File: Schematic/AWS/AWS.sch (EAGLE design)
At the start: 21 parts, among them J1 WeatherShield, J2 Fan, J3 Valve, J4 FlowMeter, Q1 IRLZ44Z, U1 SN754410_NE_16, X1 16 MHz

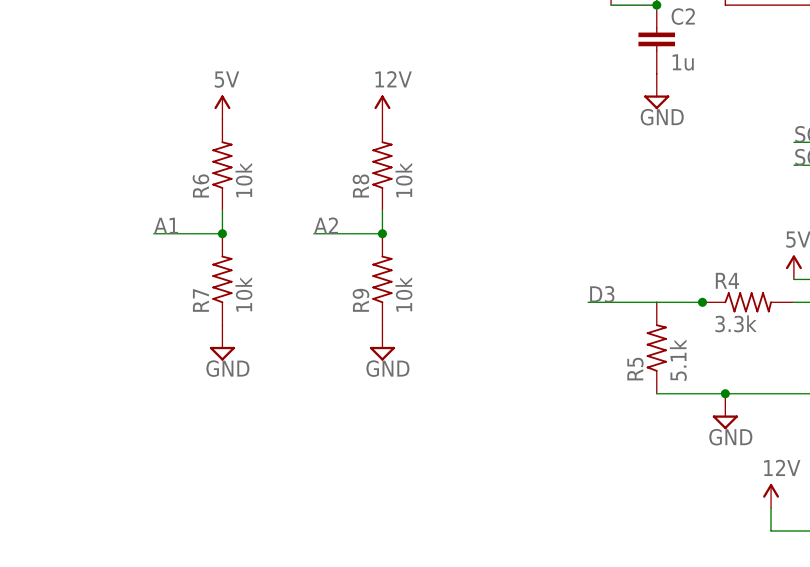
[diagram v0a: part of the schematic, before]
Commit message: Updated Resistor value
And remove .s#* files
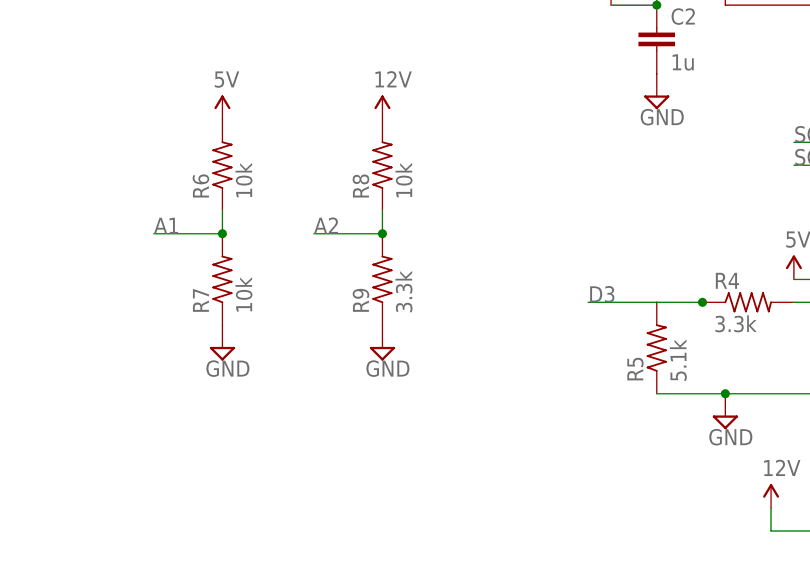
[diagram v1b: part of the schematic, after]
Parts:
- R9: value 10k -> 3.3k
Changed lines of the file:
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@@
 <part name="SUPPLY15" library="SparkFun" deviceset="VCC" device="" value="5V"/>
 <part name="R8" library="rcl" deviceset="R-US_" device="0204/2V" value="10k"/>
-<part name="R9" library="rcl" deviceset="R-US_" device="0204/2V" value="10k"/>
+<part name="R9" library="rcl" deviceset="R-US_" device="0204/2V" value="3.3k"/>
 <part name="SUPPLY16" library="supply2" deviceset="GND" device=""/>
 <part name="SUPPLY17" library="SparkFun" deviceset="VCC" device="" value="12V"/>

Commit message: Fan Working
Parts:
- removed Q1: IRLZ44Z, transistor-power:IRLZ44Z
- removed R3: 330, rcl:R-US_0204/2V
- R7: value 10k -> 2.2k
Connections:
- removed net N$4: J2.3, Q1.D
- removed net N$5: C1.2, U1.GND_1, U1.GND_4
- removed net N$8: Q1.G, R3.2
- new net FAN: J2.2, U1.3Y
- net A0: now also U1.3A; no longer R3.1
- net A1: now also U1.3; no longer R6.1, R7.2
- net A6: now also R6.1, R7.2
- net GND: now also C1.2, J2.3, U1.GND_1, U1.GND_4; no longer Q1.S
- net VCC: no longer J2.1
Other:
- moved on the sheet: C1
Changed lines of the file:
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@@
 <part name="SUPPLY9" library="SparkFun" deviceset="VCC" device="" value="5V"/>
 <part name="SUPPLY10" library="supply2" deviceset="GND" device=""/>
-<part name="Q1" library="transistor-power" deviceset="IRLZ44Z" device=""/>
 <part name="J2" library="con-amp" deviceset="215876-6" device="" value="Fan"/>
-<part name="SUPPLY11" library="SparkFun" deviceset="VCC" device="" value="12V"/>
-<part name="SUPPLY12" library="supply2" deviceset="GND" device=""/>
-<part name="R3" library="rcl" deviceset="R-US_" device="0204/2V" value="330"/>
 <part name="R4" library="rcl" deviceset="R-US_" device="0204/2V" value="3.3k"/>
 <part name="R5" library="rcl" deviceset="R-US_" device="0204/2V" value="5.1k"/>
 <part name="R6" library="rcl" deviceset="R-US_" device="0204/2V" value="10k"/>
-<part name="R7" library="rcl" deviceset="R-US_" device="0204/2V" value="10k"/>
+<part name="R7" library="rcl" deviceset="R-US_" device="0204/2V" value="2.2k"/>
 <part name="SUPPLY13" library="supply2" deviceset="GND" device=""/>
 <part name="SUPPLY15" library="SparkFun" deviceset="VCC" device="" value="5V"/>
@@
 <part name="SUPPLY16" library="supply2" deviceset="GND" device=""/>
 <part name="SUPPLY17" library="SparkFun" deviceset="VCC" device="" value="12V"/>
+<part name="SUPPLY11" library="supply2" deviceset="GND" device=""/>
 </parts>
 <sheets>
@@
 </instance>
 <instance part="U1" gate="A" x="220.98" y="134.62"/>
-<instance part="SUPPLY2" gate="1" x="243.84" y="147.32"/>
+<instance part="SUPPLY2" gate="1" x="248.92" y="147.32"/>
 <instance part="SUPPLY1" gate="GND" x="185.42" y="129.54"/>
-<instance part="SUPPLY3" gate="GND" x="243.84" y="129.54"/>
+<instance part="SUPPLY3" gate="GND" x="248.92" y="132.08"/>
 <instance part="SUPPLY7" gate="1" x="198.12" y="119.38"/>
-<instance part="C1" gate="G$1" x="243.84" y="139.7"/>
+<instance part="C1" gate="G$1" x="248.92" y="139.7"/>
 <instance part="C2" gate="G$1" x="203.2" y="116.84"/>
 <instance part="SUPPLY8" gate="GND" x="203.2" y="109.22"/>
@@
 <instance part="SUPPLY9" gate="1" x="218.44" y="88.9"/>
 <instance part="SUPPLY10" gate="GND" x="210.82" y="73.66"/>
-<instance part="Q1" gate="G$1" x="208.28" y="50.8"/>
 <instance part="J2" gate="G$1" x="228.6" y="55.88"/>
-<instance part="SUPPLY11" gate="1" x="215.9" y="63.5"/>
-<instance part="SUPPLY12" gate="GND" x="210.82" y="43.18"/>
-<instance part="R3" gate="G$1" x="198.12" y="48.26"/>
 <instance part="R4" gate="G$1" x="213.36" y="86.36"/>
 <instance part="R5" gate="G$1" x="203.2" y="81.28" rot="R90"/>
@@
 <instance part="SUPPLY16" gate="GND" x="172.72" y="81.28"/>
 <instance part="SUPPLY17" gate="1" x="172.72" y="106.68"/>
+<instance part="SUPPLY11" gate="GND" x="218.44" y="50.8"/>
 </instances>
 <busses>
@@
 </segment>
 <segment>
-<pinref part="Q1" gate="G$1" pin="S"/>
-<pinref part="SUPPLY12" gate="GND" pin="GND"/>
-</segment>
-<segment>
 <pinref part="R5" gate="G$1" pin="1"/>
 <pinref part="SUPPLY10" gate="GND" pin="GND"/>
@@
 <pinref part="R9" gate="G$1" pin="1"/>
 <pinref part="SUPPLY16" gate="GND" pin="GND"/>
+</segment>
+<segment>
+<pinref part="U1" gate="A" pin="GND_4"/>
+<pinref part="U1" gate="A" pin="GND_1"/>
+<wire x1="238.76" y1="132.08" x2="238.76" y2="134.62" width="0.1524" layer="91"/>
+<wire x1="238.76" y1="134.62" x2="248.92" y2="134.62" width="0.1524" layer="91"/>
+<pinref part="C1" gate="G$1" pin="2"/>
+<junction x="248.92" y="134.62"/>
+<pinref part="SUPPLY3" gate="GND" pin="GND"/>
+</segment>
+<segment>
+<pinref part="J2" gate="G$1" pin="3"/>
+<pinref part="SUPPLY11" gate="GND" pin="GND"/>
+<wire x1="226.06" y1="55.88" x2="218.44" y2="55.88" width="0.1524" layer="91"/>
+<wire x1="218.44" y1="55.88" x2="218.44" y2="53.34" width="0.1524" layer="91"/>
 </segment>
 </net>
@@
 <segment>
 <pinref part="U1" gate="A" pin="VCC1"/>
-<wire x1="238.76" y1="142.24" x2="243.84" y2="142.24" width="0.1524" layer="91"/>
+<wire x1="238.76" y1="142.24" x2="248.92" y2="142.24" width="0.1524" layer="91"/>
 <pinref part="SUPPLY2" gate="1" pin="VCC"/>
-<wire x1="243.84" y1="142.24" x2="243.84" y2="147.32" width="0.1524" layer="91"/>
+<wire x1="248.92" y1="142.24" x2="248.92" y2="147.32" width="0.1524" layer="91"/>
 <pinref part="C1" gate="G$1" pin="1"/>
-<junction x="243.84" y="142.24"/>
+<junction x="248.92" y="142.24"/>
 </segment>
 <segment>
@@
 </segment>
 <segment>
-<pinref part="J2" gate="G$1" pin="1"/>
-<pinref part="SUPPLY11" gate="1" pin="VCC"/>
-<wire x1="226.06" y1="60.96" x2="215.9" y2="60.96" width="0.1524" layer="91"/>
-<wire x1="215.9" y1="60.96" x2="215.9" y2="63.5" width="0.1524" layer="91"/>
-</segment>
-<segment>
 <pinref part="R8" gate="G$1" pin="2"/>
 <pinref part="SUPPLY17" gate="1" pin="VCC"/>
@@
 <pinref part="ATMEGA328" gate="G$1" pin="ADC6"/>
 </segment>
+<segment>
+<pinref part="R6" gate="G$1" pin="1"/>
+<pinref part="R7" gate="G$1" pin="2"/>
+<wire x1="154.94" y1="96.52" x2="154.94" y2="93.98" width="0.1524" layer="91"/>
+<wire x1="154.94" y1="93.98" x2="147.32" y2="93.98" width="0.1524" layer="91"/>
+<junction x="154.94" y="93.98"/>
+<label x="147.32" y="93.98" size="1.778" layer="95"/>
+</segment>
 </net>
 <net name="A4_SDA" class="0">
@@
 </segment>
 <segment>
-<pinref part="R6" gate="G$1" pin="1"/>
-<pinref part="R7" gate="G$1" pin="2"/>
-<wire x1="154.94" y1="96.52" x2="154.94" y2="93.98" width="0.1524" layer="91"/>
-<wire x1="154.94" y1="93.98" x2="147.32" y2="93.98" width="0.1524" layer="91"/>
-<junction x="154.94" y="93.98"/>
-<label x="147.32" y="93.98" size="1.778" layer="95"/>
+<pinref part="U1" gate="A" pin="3"/>
+<wire x1="238.76" y1="124.46" x2="243.84" y2="124.46" width="0.1524" layer="91"/>
+<label x="241.3" y="124.46" size="1.778" layer="95"/>
 </segment>
 </net>
@@
 </segment>
 <segment>
-<pinref part="R3" gate="G$1" pin="1"/>
-<wire x1="193.04" y1="48.26" x2="185.42" y2="48.26" width="0.1524" layer="91"/>
-<label x="185.42" y="48.26" size="1.778" layer="95"/>
+<pinref part="U1" gate="A" pin="3A"/>
+<wire x1="238.76" y1="127" x2="243.84" y2="127" width="0.1524" layer="91"/>
+<label x="241.3" y="127" size="1.778" layer="95"/>
 </segment>
 </net>
@@
 </segment>
 </net>
-<net name="N$5" class="0">
-<segment>
-<pinref part="U1" gate="A" pin="GND_4"/>
-<pinref part="U1" gate="A" pin="GND_1"/>
-<wire x1="238.76" y1="132.08" x2="238.76" y2="134.62" width="0.1524" layer="91"/>
-<wire x1="238.76" y1="134.62" x2="243.84" y2="134.62" width="0.1524" layer="91"/>
-<wire x1="243.84" y1="134.62" x2="243.84" y2="132.08" width="0.1524" layer="91"/>
-<pinref part="C1" gate="G$1" pin="2"/>
-<junction x="243.84" y="134.62"/>
-</segment>
-</net>
 <net name="SOL+" class="0">
 <segment>
@@
 </segment>
 </net>
-<net name="N$4" class="0">
-<segment>
-<pinref part="Q1" gate="G$1" pin="D"/>
-<pinref part="J2" gate="G$1" pin="3"/>
-<wire x1="210.82" y1="55.88" x2="226.06" y2="55.88" width="0.1524" layer="91"/>
-</segment>
-</net>
-<net name="N$8" class="0">
-<segment>
-<pinref part="Q1" gate="G$1" pin="G"/>
-<pinref part="R3" gate="G$1" pin="2"/>
-<wire x1="205.74" y1="48.26" x2="203.2" y2="48.26" width="0.1524" layer="91"/>
-</segment>
-</net>
+<net name="FAN" class="0">
+<segment>
+<pinref part="U1" gate="A" pin="3Y"/>
+<wire x1="238.76" y1="129.54" x2="243.84" y2="129.54" width="0.1524" layer="91"/>
+<label x="241.3" y="129.54" size="1.778" layer="95"/>
+</segment>
+<segment>
+<pinref part="J2" gate="G$1" pin="2"/>
+<wire x1="226.06" y1="58.42" x2="218.44" y2="58.42" width="0.1524" layer="91"/>
+<label x="218.44" y="58.42" size="1.778" layer="95"/>
+</segment>
+</net>

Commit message: All Basic Functions Working!
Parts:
- added R3: 10k, rcl:R-US_0204/2V
- R4: value 3.3k -> 10k
- R5: value 5.1k -> 3.3k
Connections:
- net D3: now also R3.1
- net VCC: now also R3.2
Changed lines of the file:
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@@
 <part name="J3" library="con-amp" deviceset="215876-6" device="" value="Valve"/>
 <part name="J4" library="con-amp" deviceset="215876-6" device="" value="FlowMeter"/>
-<part name="SUPPLY9" library="SparkFun" deviceset="VCC" device="" value="5V"/>
+<part name="SUPPLY9" library="SparkFun" deviceset="VCC" device="" value="12V"/>
 <part name="SUPPLY10" library="supply2" deviceset="GND" device=""/>
 <part name="J2" library="con-amp" deviceset="215876-6" device="" value="Fan"/>
-<part name="R4" library="rcl" deviceset="R-US_" device="0204/2V" value="3.3k"/>
-<part name="R5" library="rcl" deviceset="R-US_" device="0204/2V" value="5.1k"/>
+<part name="R4" library="rcl" deviceset="R-US_" device="0204/2V" value="10k"/>
+<part name="R5" library="rcl" deviceset="R-US_" device="0204/2V" value="3.3k"/>
 <part name="R6" library="rcl" deviceset="R-US_" device="0204/2V" value="10k"/>
 <part name="R7" library="rcl" deviceset="R-US_" device="0204/2V" value="2.2k"/>
@@
 <part name="SUPPLY17" library="SparkFun" deviceset="VCC" device="" value="12V"/>
 <part name="SUPPLY11" library="supply2" deviceset="GND" device=""/>
+<part name="R3" library="rcl" deviceset="R-US_" device="0204/2V" value="10k"/>
 </parts>
 <sheets>
@@
 <instance part="J3" gate="G$1" x="228.6" y="101.6"/>
 <instance part="J4" gate="G$1" x="228.6" y="83.82"/>
-<instance part="SUPPLY9" gate="1" x="218.44" y="88.9"/>
+<instance part="SUPPLY9" gate="1" x="213.36" y="93.98"/>
 <instance part="SUPPLY10" gate="GND" x="210.82" y="73.66"/>
 <instance part="J2" gate="G$1" x="228.6" y="55.88"/>
@@
 <instance part="SUPPLY17" gate="1" x="172.72" y="106.68"/>
 <instance part="SUPPLY11" gate="GND" x="218.44" y="50.8"/>
+<instance part="R3" gate="G$1" x="205.74" y="93.98"/>
 </instances>
 <busses>
@@
 </segment>
 <segment>
-<pinref part="J4" gate="G$1" pin="1"/>
-<wire x1="226.06" y1="88.9" x2="218.44" y2="88.9" width="0.1524" layer="91"/>
-<pinref part="SUPPLY9" gate="1" pin="VCC"/>
-</segment>
-<segment>
 <pinref part="R8" gate="G$1" pin="2"/>
 <pinref part="SUPPLY17" gate="1" pin="VCC"/>
@@
 <pinref part="R6" gate="G$1" pin="2"/>
 <pinref part="SUPPLY15" gate="1" pin="VCC"/>
+</segment>
+<segment>
+<pinref part="SUPPLY9" gate="1" pin="VCC"/>
+<wire x1="213.36" y1="93.98" x2="213.36" y2="88.9" width="0.1524" layer="91"/>
+<pinref part="J4" gate="G$1" pin="1"/>
+<wire x1="213.36" y1="88.9" x2="226.06" y2="88.9" width="0.1524" layer="91"/>
+<pinref part="R3" gate="G$1" pin="2"/>
+<wire x1="210.82" y1="93.98" x2="213.36" y2="93.98" width="0.1524" layer="91"/>
+<junction x="213.36" y="93.98"/>
 </segment>
 </net>
@@
 <junction x="208.28" y="86.36"/>
 <label x="195.58" y="86.36" size="1.778" layer="95"/>
-<wire x1="203.2" y1="86.36" x2="195.58" y2="86.36" width="0.1524" layer="91"/>
+<wire x1="203.2" y1="86.36" x2="200.66" y2="86.36" width="0.1524" layer="91"/>
+<wire x1="200.66" y1="86.36" x2="195.58" y2="86.36" width="0.1524" layer="91"/>
 <wire x1="208.28" y1="86.36" x2="203.2" y2="86.36" width="0.1524" layer="91"/>
-</segment>
-</net>
+<pinref part="R3" gate="G$1" pin="1"/>
+<wire x1="200.66" y1="93.98" x2="200.66" y2="86.36" width="0.1524" layer="91"/>
+<junction x="200.66" y="86.36"/>
+</segment>
+</net>
